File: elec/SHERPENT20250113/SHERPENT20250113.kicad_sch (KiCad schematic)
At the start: 128 parts, among them J1 2137160001, J2 Conn_01x02_Socket, J3 Conn_01x03_Socket, J4 Conn_01x03_Socket, Q1 NMOS, Q101 PMOS, Q2 PMOS, SW1 SW_Push, SW101 SW_Push, U1 AN034_ANTENNA, U2 MCP73831T-2ACI_OT, U3 TPS61288LRQQR, U4 TPS7A2633DRVR, U5 LM66200DRLR, U6 ESP32-C3, U7 W25Q128JVS, Y1 40MHz

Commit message: shema bo
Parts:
- removed D109, D110, D111, D112, D113, D114, D115, D116, D12, D125, D126, D127, D128, D129, D13, D14, D15, D16, D17, D18, D19: WS2812B4020, Library:WS2812B4020, symbol WS2812B4020:WS2812B
- removed D119, D120, D121: WS2812B, LED_SMD:LED_WS2812B_PLCC4_5.0x5.0mm_P3.2mm, symbol LED:WS2812B
- removed J2: Conn_01x02_Socket, Connector_PinSocket_2.54mm:PinSocket_1x02_P2.54mm_Vertical, symbol Connector:Conn_01x02_Socket
- removed TP10, TP101, TP102: TestPoint, TestPoint:TestPoint_Pad_D1.5mm, symbol Connector:TestPoint
- added BT2: Battery_Cell, Connector_PinHeader_2.54mm:PinHeader_1x02_P2.54mm_Vertical, symbol Device:Battery_Cell
- added C10, C9: 1u, symbol Device:C
- added C7, C8: 100u, symbol Device:C_Polarized
- added D1: D_Schottky, LED_SMD:LED_0603_1608Metric_Pad1.05x0.95mm_HandSolder, symbol Device:D_Schottky
- added NEO-END: TestPoint, TestPoint:TestPoint_Loop_D2.54mm_Drill1.5mm_Beaded, symbol Connector:TestPoint
- added Q1: NMOS, Package_TO_SOT_SMD:SOT-23, symbol Simulation_SPICE:NMOS
- added R1: 10k, Resistor_SMD:R_0603_1608Metric, symbol Device:R_US
- added U4: LD1117S50TR_SOT223, Package_TO_SOT_SMD:SOT-223-3_TabPin2, symbol Regulator_Linear:LD1117S50TR_SOT223
- D5: renamed from D20; now not fitted; now left out of the parts list
- R15: renamed from R22; now not fitted; now left out of the parts list
- U3: renamed from U5; now not fitted
- renumbered C12 to C1, C4 to C11, C5 to C12, C6 to C13, C25 to C14, C9 to C15, C10 to C16, C8 to C17, C13 to C18, C15 to C19, C7 to C2, C16 to C20, C18 to C21, C17 to C22, C19 to C23, C14 to C24, C20 to C25, C21 to C26, C22 to C27, C23 to C28, C24 to C29, C2 to C3, C11 to C4, C1 to C5, C3 to C6, D102 to D10, D118 to D11, D3 to D12, D6 to D13, D103 to D14, D7 to D16, D104 to D17, D8 to D19, D122 to D2, D105 to D20, D9 to D22, D106 to D23, D10 to D24, D107 to D25, D11 to D26, D108 to D27, D1 to D3, D2 to D4, D4 to D6, D101 to D7, D117 to D8, D5 to D9, J3 to J2, J4 to J3, Q1 to Q3, Q101 to Q4, R24 to R10, R1 to R11, R3 to R12, R2 to R13, R7 to R14, R15 to R16, R11 to R17, R14 to R18, R12 to R19, R26 to R2, R13 to R20, R16 to R21, R17 to R22, R18 to R23, R19 to R24, R20 to R25, R21 to R26, R5 to R3, R103 to R4, R101 to R5, R102 to R6, R8 to R7, R9 to R8, R6 to R9, SW101 to SW1, SW1 to SW2, TP7 to TP3, TP8 to TP4, TP4 to TP5, TP9 to TP6, U2 to U1, U3 to U2, U4 to U5, U1 to U6, U6 to U7, U7 to U8
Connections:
- net +3.3V: now also R1.1
- net +5V: now also U4.2 (VO); no longer D10.1 (VDD), D11.1 (VDD), D13.1 (VDD), D14.1 (VDD), D16.1 (VDD), D17.1 (VDD), D19.1 (VDD), D20.1 (VDD), D22.1 (VDD), D23.1 (VDD), D24.1 (VDD), D25.1 (VDD), D26.1 (VDD), D27.1 (VDD), D6.1 (VDD), D7.1 (VDD), D8.1 (VDD), D9.1 (VDD)
- net +9V: now also C10.1, C7.1, C8.1, C9.1, U4.3 (VI)
- net Button: now also Q1.1 (D), R1.2; no longer D2.1 (K), R4.2, SW1.2
- net CHARGE: now also Q2.1 (D), R2.2; no longer R2.1
- net GND: now also R2.1, BT2.2 (-), C10.2, C7.2, C8.2, C9.2, Q1.3 (S)
- net I2C_DO: no longer D6.4 (DIN), D7.4 (DIN), D8.4 (DIN)
- net StayOn: now also D1.2 (A); no longer Q3.2 (G), R5.1
- net USB_ESP32N: now also TP5.1
- net VUSB: now also Q3.2 (G), R5.1, D1.1 (K)
- net at D27.2 (DOUT): now also D11.4 (DIN)
- net at D26.2 (DOUT): now also D8.4 (DIN)
- net at BT1.1 (+), F1.1: now also BT2.1 (+)
- net NEO_Row2: now reaches D8.2 (DOUT)
- net NEO_Row2: now also D7.4 (DIN); no longer D11.4 (DIN)
- net at D11.2 (DOUT): now also NEO-END.1
- net I2C_DI renamed NEOPX
- net NEOPX: now also D6.4 (DIN)
- new net: D2.1 (K), Q1.2 (G), R4.2, SW1.2
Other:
- note added: "3.3v Reg"
- note added: "5v Reg"
- note added: "Boost converter"
- note added: "Changements: - Stayon fonctionner - Le stayon defeat le purpose de la diode idéale - Ajouté des condensateurs pour filtrer les spikes et drops des servo - LDO pour leds - Les neopixels c pas I2C c'est un affaire qui existe juste pour ça. C'est un peu l'equivalent de juste TX mais pas exactement. J'ai enlevé le connecteur I2C et j'ai utilisé la pin de plus pour le bouton Questions: - V USB sur le 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"
- note added: "Charger"
- note added: "Connectors"
- note added: "Control"
- note added: "Filters"
- note added: "LEDs"
- note added: "MCU power selector"
- note added: "Makes sure the MCU wakes up when usb is plugged in !! USP at stayon defeats the purpose of this part"
- note added: "Motors"
- note added: "À vérifier"
- note removed: "Connecteur Moteur"
- moved on the sheet: BT1, C1, C11, C12, C13, C14, C15, C16, C17, C18, C19, C2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

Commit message: Amélioration du shema. Layout et routing de tout ce qui manquait sauf leds et bouton. Bonne nuit!
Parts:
- added D25: D_Schottky, LED_SMD:LED_0603_1608Metric_Pad1.05x0.95mm_HandSolder, symbol Device:D_Schottky
- U4: now not fitted; now left out of the parts list
- renumbered C17 to C16, C18 to C17, C19 to C18, C20 to C19, C21 to C20, C16 to C21, D13 to D11, D14 to D12, D16 to D13, D17 to D14, D19 to D15, D20 to D16, D22 to D17, D23 to D18, D24 to D19, D25 to D20, D26 to D21, D27 to D22, D8 to D23, D11 to D24, D12 to D6, D6 to D7, D7 to D8, NEO-END to NEO-END1, R9 to R10, R4 to R3, R3 to R4, R10 to R9
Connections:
- net VUSB: now also D25.2 (A); no longer D1.1 (K), Q3.2 (G), R5.1
- new net: D1.1 (K), D25.1 (K), Q3.2 (G), R5.1

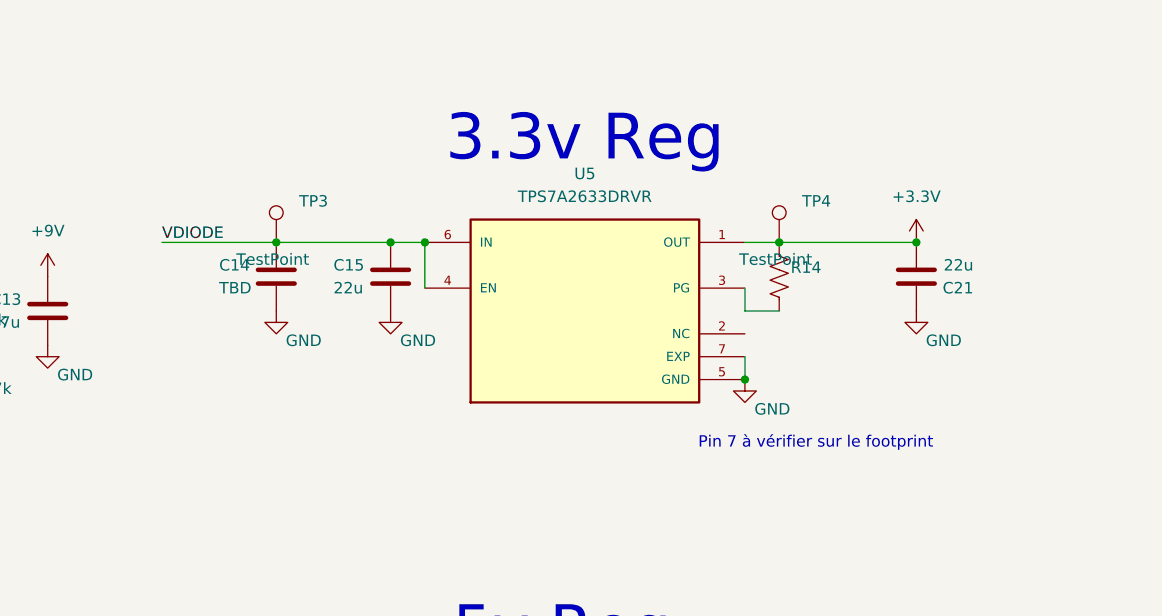
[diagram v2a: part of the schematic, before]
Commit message: Ajout de datasheet et changement de LDO
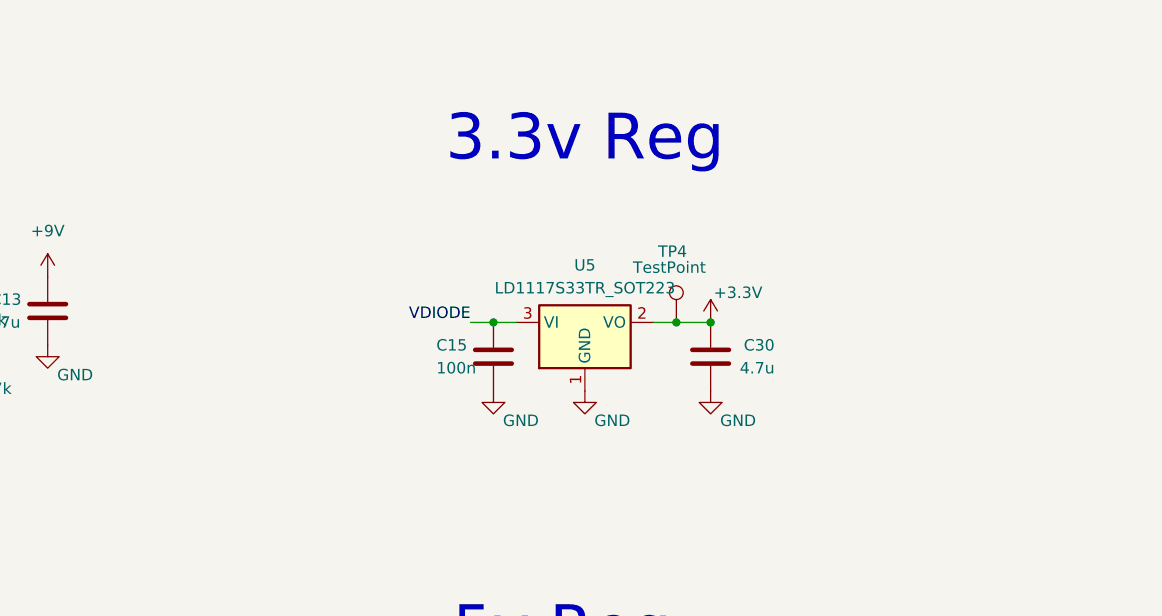
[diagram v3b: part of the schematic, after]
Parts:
- removed C14: TBD, Capacitor_SMD:C_0603_1608Metric_Pad1.08x0.95mm_HandSolder, symbol Device:C
- removed C21: 22u, Capacitor_SMD:C_0603_1608Metric_Pad1.08x0.95mm_HandSolder, symbol Device:C
- removed R14: 100k, Resistor_SMD:R_0603_1608Metric, symbol Device:R_US
- removed TP3: TestPoint, TestPoint:TestPoint_Loop_D2.54mm_Drill1.5mm_Beaded, symbol Connector:TestPoint
- removed U5: TPS7A2633DRVR, TPS7A2633DRVR:SON65P200X200X80-7N, symbol TPS7A2633DRVR:TPS7A2633DRVR
- added C30: 4.7u, Capacitor_SMD:C_0603_1608Metric_Pad1.08x0.95mm_HandSolder, symbol Device:C
- added U5: LD1117S33TR_SOT223, Package_TO_SOT_SMD:SOT-223-3_TabPin2, symbol Regulator_Linear:LD1117S33TR_SOT223
- C10, C7, C8, C9: footprint (none) -> Capacitor_SMD:C_0603_1608Metric_Pad1.08x0.95mm_HandSolder
- C15: value 22u -> 100n
- J2, J3: footprint Connector_PinSocket_2.54mm:PinSocket_1x03_P2.54mm_Vertical -> Connector_PinHeader_2.54mm:PinHeader_1x03_P2.54mm_Vertical
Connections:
- net +3.3V: now also C30.2, U5.2 (VO)
- net GND: now also C30.1, U5.1 (GND)
- net VDIODE: now also U5.3 (VI)
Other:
- note removed: "Pin 7 à vérifier sur le footprint"
- moved on the sheet: C15, TP4

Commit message: Bouton placé
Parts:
- removed SW1: SW_Push, CS1213AGF160:SW_CS1213AG_CRS, symbol Switch:SW_Push
- added SW1: CT1102, CT1102V3.15F100:CT1102V3.15F100, symbol CT1120V3.15F100:buttonwithgnds
- renumbered D13 to D10, D15 to D11, D17 to D12, D19 to D13, D21 to D14, D23 to D15, D8 to D16, D10 to D17, D12 to D18, D14 to D19, D16 to D20, D18 to D21, D20 to D22, D22 to D23, D9 to D8, D11 to D9
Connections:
- net GND: now also SW1.1, SW1.3, SW1.4
- net at D2.1 (K), Q1.2 (G), R3.2: now also SW1.2
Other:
- moved on the sheet: Q1, R1

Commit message: Tiens max have fun
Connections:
- net +5V: now also D10.1 (VDD), D11.1 (VDD), D12.1 (VDD), D13.1 (VDD), D14.1 (VDD), D15.1 (VDD), D16.1 (VDD), D17.1 (VDD), D18.1 (VDD), D19.1 (VDD), D20.1 (VDD), D21.1 (VDD), D22.1 (VDD), D23.1 (VDD), D24.1 (VDD), D7.1 (VDD), D8.1 (VDD), D9.1 (VDD)
- net GND: no longer J1.SH1 (SHIELD1), J1.SH2 (SHIELD2), J1.SH3 (SHIELD3), J1.SH4 (SHIELD4)
- no-connect marks 0 -> 6

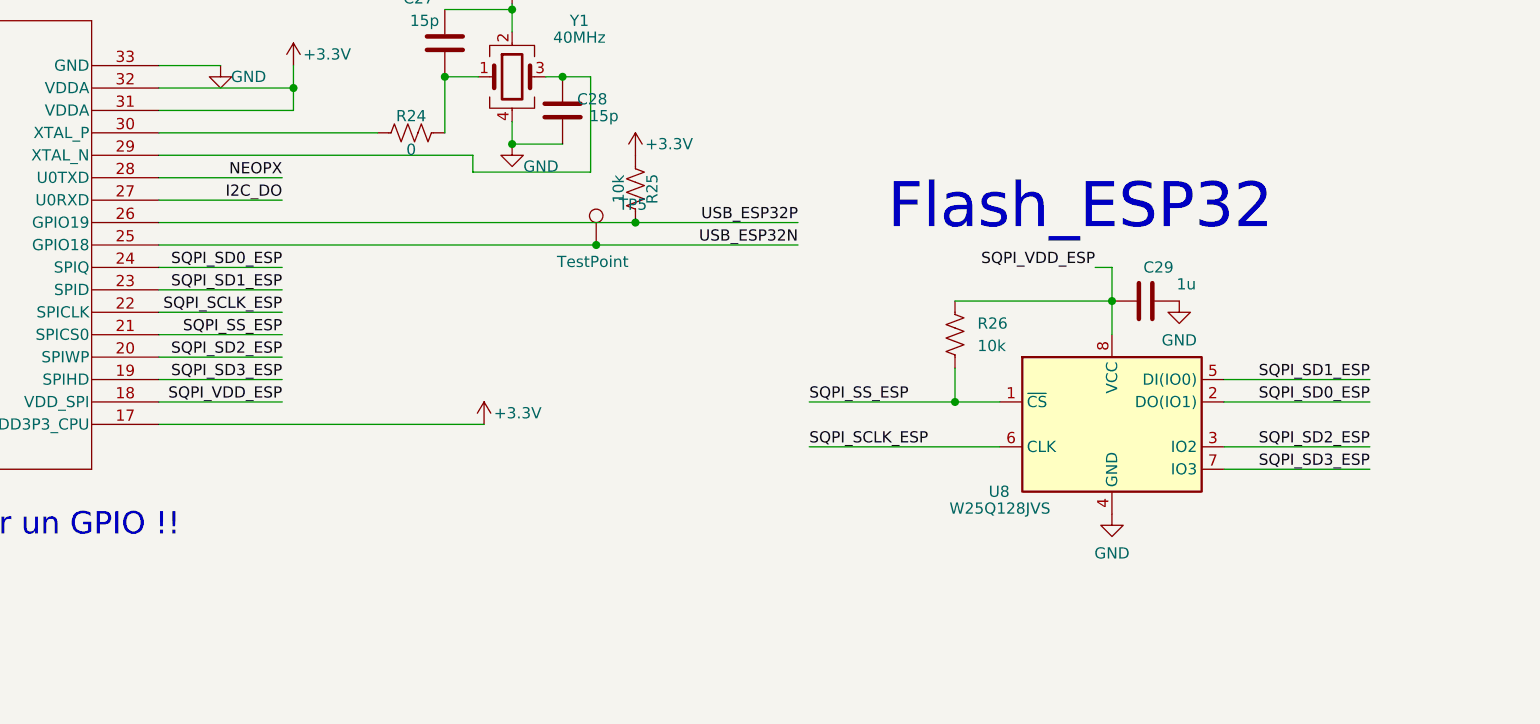
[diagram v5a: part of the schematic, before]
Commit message: Changement de place de l'ESP
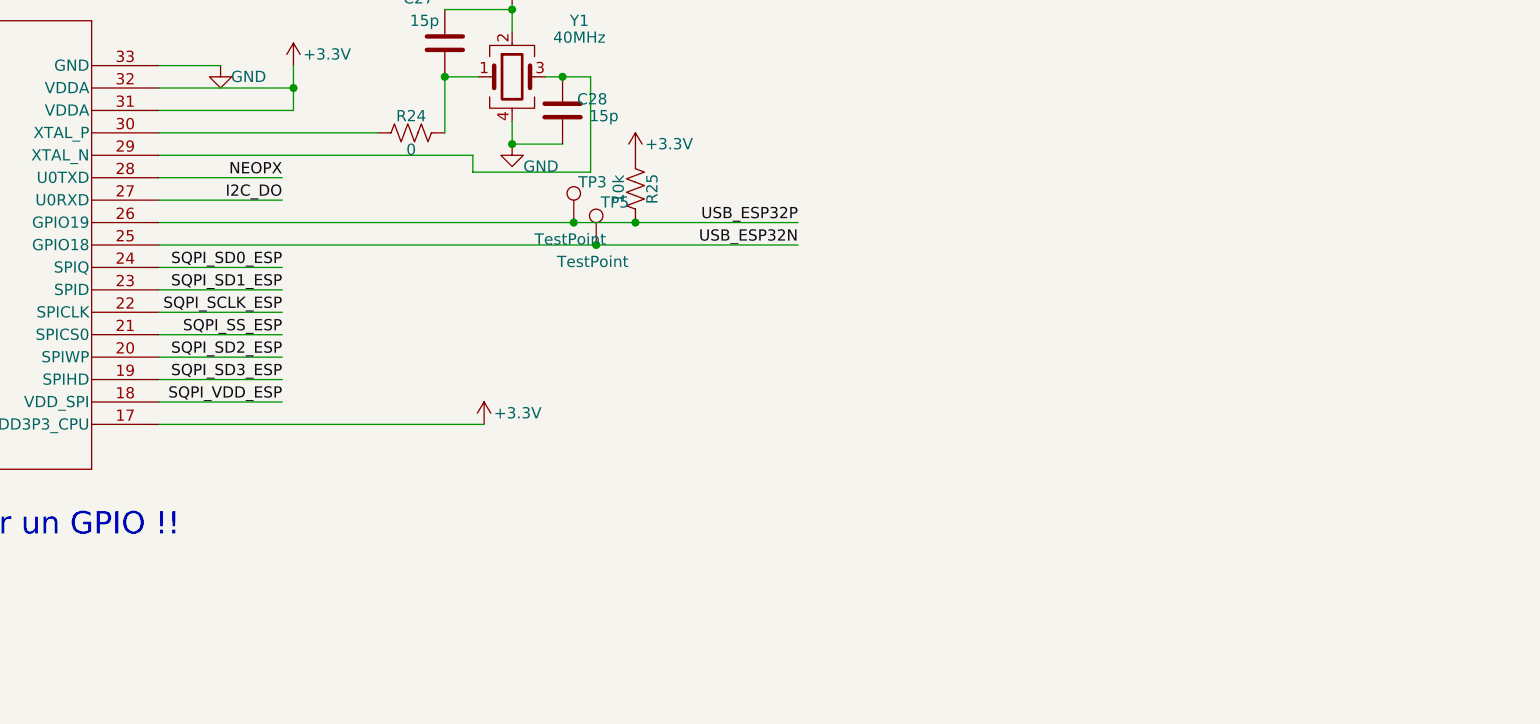
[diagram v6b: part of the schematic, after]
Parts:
- removed C29: 1u, Capacitor_SMD:C_0603_1608Metric_Pad1.08x0.95mm_HandSolder, symbol Device:C
- removed R26: 10k, Resistor_SMD:R_0603_1608Metric, symbol Device:R_US
- removed U8: W25Q128JVS, W25Q128JVSIQ:SOIC_128JVSIQ_WIN-L, symbol Memory_Flash:W25Q128JVS
- added TP3: TestPoint, TestPoint:TestPoint_Loop_D2.54mm_Drill1.5mm_Beaded, symbol Connector:TestPoint
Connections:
- net USB_ESP32P: now also TP3.1
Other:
- note removed: "Flash_ESP32"

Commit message: PCB finie, il reste le DRC
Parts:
- added H1, H2, H3, H4: MountingHole, MountingHole:MountingHole_2.7mm_M2.5, symbol Mechanical:MountingHole
- added JP1, JP10, JP11, JP12, JP13, JP14, JP15, JP16, JP17, JP18, JP2, JP3, JP4, JP5, JP6, JP7, JP8, JP9: SolderJumper_2_Open, Jumper:SolderJumper-2_P1.3mm_Open_TrianglePad1.0x1.5mm, symbol Jumper:SolderJumper_2_Open
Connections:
- net NEOPX: now also JP1.1 (A)
- net NEO_Row2: now also JP18.1 (A), JP9.2 (B)
- net at D23.2 (DOUT), D24.4 (DIN): now also JP10.1 (A), JP11.2 (B)
- net at D22.2 (DOUT), D23.4 (DIN): now also JP11.1 (A), JP12.2 (B)
- net at D24.2 (DOUT), NEO-END1.1: now also JP10.2 (B)
- net at D11.2 (DOUT), D12.4 (DIN): now also JP5.2 (B), JP6.1 (A)
- net at D10.2 (DOUT), D11.4 (DIN): now also JP4.2 (B), JP5.1 (A)
- net at D10.4 (DIN), D9.2 (DOUT): now also JP3.2 (B), JP4.1 (A)
- net at D8.2 (DOUT), D9.4 (DIN): now also JP2.2 (B), JP3.1 (A)
- net at D21.2 (DOUT), D22.4 (DIN): now also JP12.1 (A), JP13.2 (B)
- net at D20.2 (DOUT), D21.4 (DIN): now also JP13.1 (A), JP14.2 (B)
- net at D19.2 (DOUT), D20.4 (DIN): now also JP14.1 (A), JP15.2 (B)
- net at D17.2 (DOUT), D18.4 (DIN): now also JP16.1 (A), JP17.2 (B)
- net at D16.2 (DOUT), D17.4 (DIN): now also JP17.1 (A), JP18.2 (B)
- net at D18.2 (DOUT), D19.4 (DIN): now also JP15.1 (A), JP16.2 (B)
- net at D14.2 (DOUT), D15.4 (DIN): now also JP8.2 (B), JP9.1 (A)
- net at D13.2 (DOUT), D14.4 (DIN): now also JP7.2 (B), JP8.1 (A)
- net at D7.2 (DOUT), D8.4 (DIN): now also JP1.2 (B), JP2.1 (A)
- net at D12.2 (DOUT), D13.4 (DIN): now also JP6.2 (B), JP7.1 (A)

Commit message: Vérification de la charge des batterie et début du sizing des via/track
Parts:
- added R14: 100k, Resistor_SMD:R_0603_1608Metric, symbol Device:R_US
- C1, C4: value 22u -> 4.7u
- D20, D21, D22, D23, D24, JP10, JP11, JP12, JP13, JP14: now not fitted
- R2: value 10k -> 100k
- R7: value 36k -> 470
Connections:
- net +5V: no longer D10.1 (VDD), D11.1 (VDD), D12.1 (VDD), D13.1 (VDD), D14.1 (VDD), D15.1 (VDD), D16.1 (VDD), D17.1 (VDD), D18.1 (VDD), D19.1 (VDD), D7.1 (VDD), D8.1 (VDD), D9.1 (VDD)
- net +9V: now also D10.1 (VDD), D11.1 (VDD), D12.1 (VDD), D13.1 (VDD), D14.1 (VDD), D15.1 (VDD), D16.1 (VDD), D17.1 (VDD), D18.1 (VDD), D19.1 (VDD), D7.1 (VDD), D8.1 (VDD), D9.1 (VDD)
- net VUSB: now also R14.2
- net at D19.2 (DOUT), D20.4 (DIN), JP14.1 (A)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: now also NEO-END1.1
- net at D24.2 (DOUT), JP10.2 (B): no longer NEO-END1.1
- net at D3.1 (K), Q2.2 (G), U1.1 (STAT): now also R14.1
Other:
- note added: "Chargeur"
- note removed: "Charger"
- moved on the sheet: NEO-END1, Q2, R2
